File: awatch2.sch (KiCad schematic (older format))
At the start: 0 parts

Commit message: add sensors
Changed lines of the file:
@@
 F35 "NRF_CHICKEN3" B L 3500 4400 50
 F36 "PMIC_INTn" I L 3500 3800 50
+F37 "SENS_IMU_INT" I R 5000 4100 50
 $EndSheet
 $Sheet
@@
 	5300 2300 5000 2300
 $Sheet
-S 5250 3800 750  600
+S 5250 3800 700  400
 U 5C3CD34E
 F0 "Sensors" 50
 F1 "awatch-sensors.sch" 50
+F2 "SENS_SCL" I L 5250 3900 50
+F3 "SENS_SDA" B L 5250 4000 50
+F4 "SENS_IMU_INT" O L 5250 4100 50
 $EndSheet
+Wire Wire Line
+	5250 3900 5000 3900
+Wire Wire Line
+	5250 4000 5000 4000
+Wire Wire Line
+	5250 4100 5000 4100
 $EndSCHEMATC

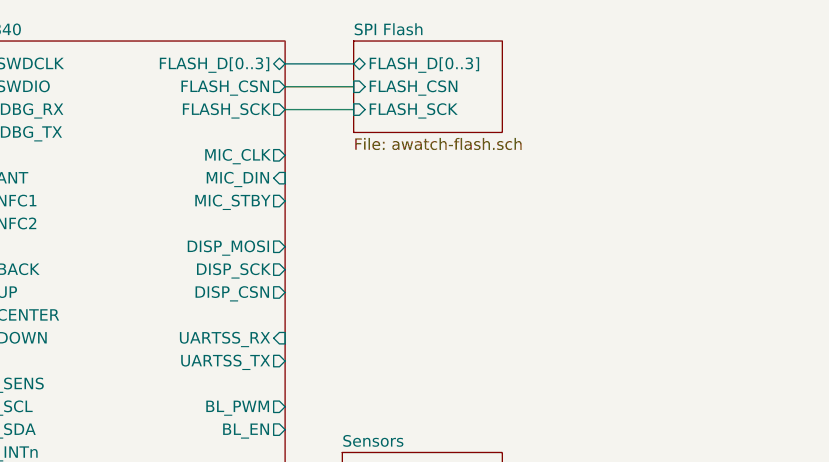
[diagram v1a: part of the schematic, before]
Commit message: add mic
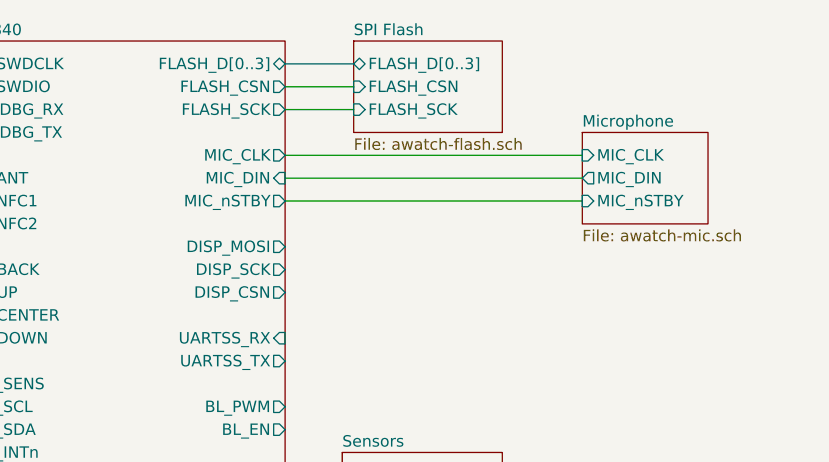
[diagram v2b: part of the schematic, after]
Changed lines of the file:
@@
 $Descr A4 11693 8268
 encoding utf-8
-Sheet 1 5
+Sheet 1 6
 Title "AWatch2"
 Date ""
@@
 F13 "MIC_CLK" O R 5000 2500 50
 F14 "MIC_DIN" I R 5000 2600 50
-F15 "MIC_STBY" O R 5000 2700 50
+F15 "MIC_nSTBY" O R 5000 2700 50
 F16 "PMIC_SCL" O L 3500 3600 50
 F17 "PMIC_SDA" B L 3500 3700 50
@@
 Wire Wire Line
 	5250 4100 5000 4100
+$Sheet
+S 6300 2400 550  400
+U 5C4541B3
+F0 "Microphone" 50
+F1 "awatch-mic.sch" 50
+F2 "MIC_nSTBY" I L 6300 2700 50
+F3 "MIC_CLK" I L 6300 2500 50
+F4 "MIC_DIN" O L 6300 2600 50
+$EndSheet
+Wire Wire Line
+	6300 2500 5000 2500
+Wire Wire Line
+	5000 2600 6300 2600
+Wire Wire Line
+	6300 2700 5000 2700
 $EndSCHEMATC

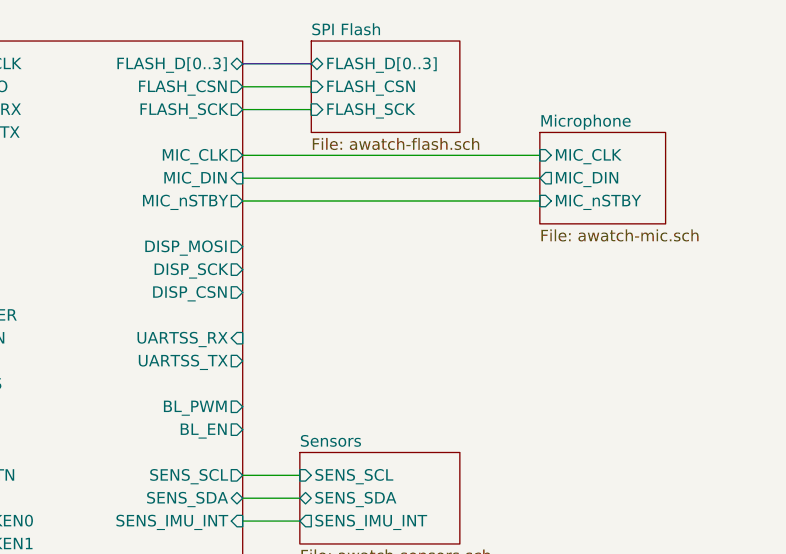
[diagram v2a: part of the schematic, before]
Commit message: Add display.  Add +3.3V LDO for backlight.
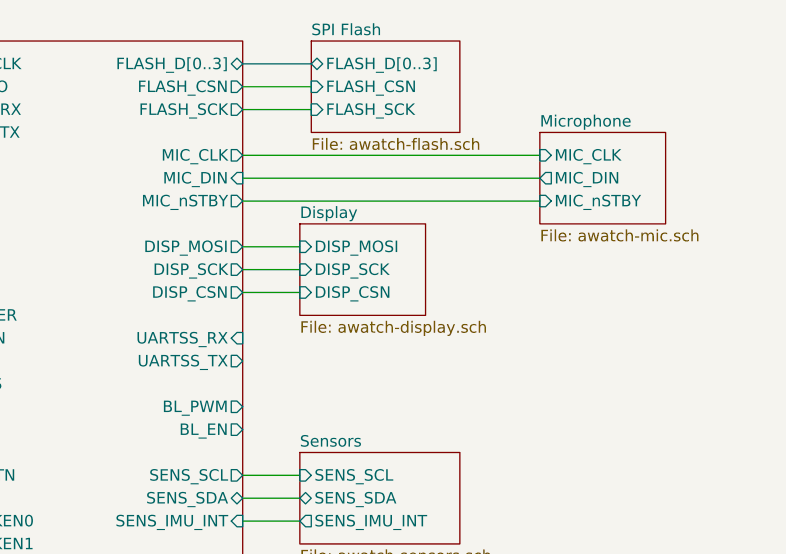
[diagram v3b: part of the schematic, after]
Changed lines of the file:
@@
 $Descr A4 11693 8268
 encoding utf-8
-Sheet 1 6
+Sheet 1 7
 Title "AWatch2"
 Date ""
@@
 Wire Wire Line
 	6300 2700 5000 2700
+$Sheet
+S 5250 2800 550  400
+U 5C4574A7
+F0 "Display" 50
+F1 "awatch-display.sch" 50
+F2 "DISP_MOSI" I L 5250 2900 50
+F3 "DISP_SCK" I L 5250 3000 50
+F4 "DISP_CSN" I L 5250 3100 50
+$EndSheet
+Wire Wire Line
+	5000 2900 5250 2900
+Wire Wire Line
+	5250 3000 5000 3000
+Wire Wire Line
+	5000 3100 5250 3100
 $EndSCHEMATC

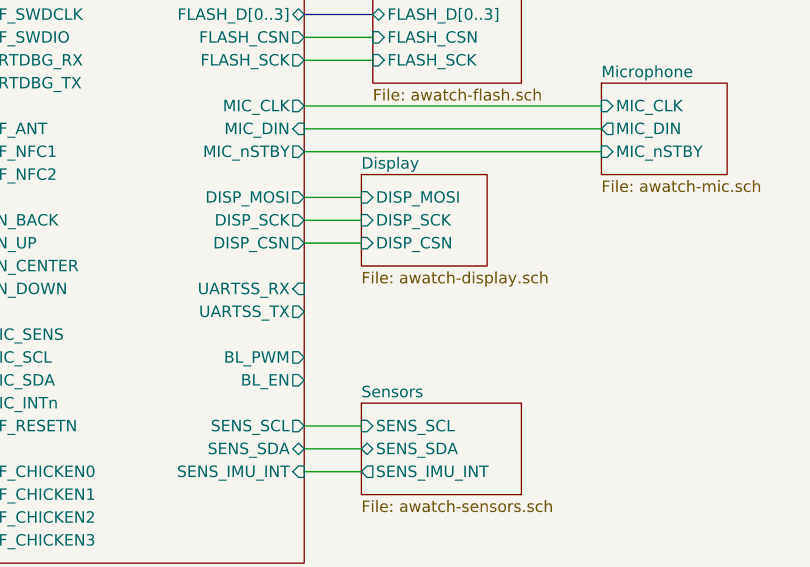
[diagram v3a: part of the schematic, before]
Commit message: backlight PWM through a FET
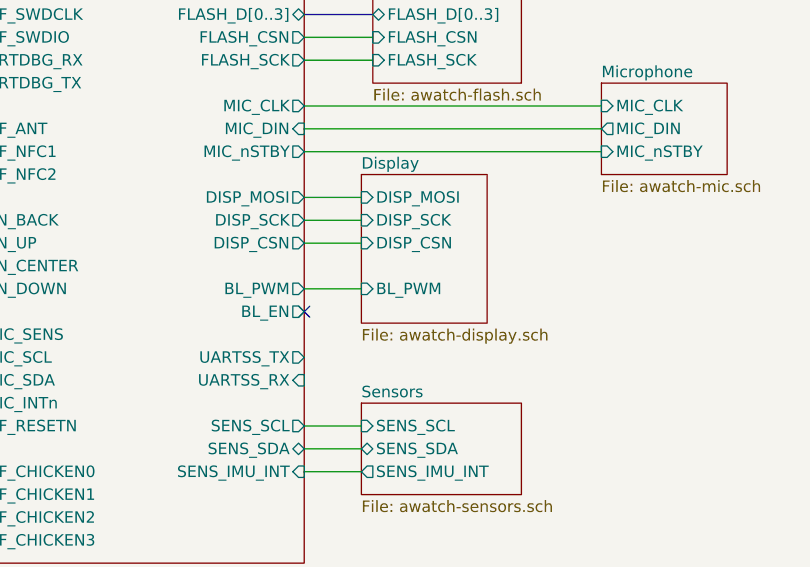
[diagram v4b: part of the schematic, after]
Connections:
- no-connect marks 0 -> 1
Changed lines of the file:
@@
 F19 "DISP_SCK" O R 5000 3000 50
 F20 "DISP_CSN" O R 5000 3100 50
-F21 "UARTSS_RX" I R 5000 3300 50
-F22 "UARTSS_TX" O R 5000 3400 50
+F21 "UARTSS_RX" I R 5000 3700 50
+F22 "UARTSS_TX" O R 5000 3600 50
 F23 "UARTDBG_RX" I L 3500 2300 50
 F24 "UARTDBG_TX" O L 3500 2400 50
-F25 "BL_PWM" O R 5000 3600 50
-F26 "BL_EN" O R 5000 3700 50
+F25 "BL_PWM" O R 5000 3300 50
+F26 "BL_EN" O R 5000 3400 50
 F27 "SENS_SCL" O R 5000 3900 50
 F28 "SENS_SDA" B R 5000 4000 50
@@
 	6300 2700 5000 2700
 $Sheet
-S 5250 2800 550  400
+S 5250 2800 550  650
 U 5C4574A7
 F0 "Display" 50
@@
 F3 "DISP_SCK" I L 5250 3000 50
 F4 "DISP_CSN" I L 5250 3100 50
+F5 "BL_PWM" I L 5250 3300 50
 $EndSheet
 Wire Wire Line
@@
 Wire Wire Line
 	5000 3100 5250 3100
+Wire Wire Line
+	5000 3300 5250 3300
+NoConn ~ 5000 3400
 $EndSCHEMATC

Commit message: add FTDI
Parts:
- added J? (x3): Conn_01x02, symbol Connector_Generic:Conn_01x02
- added SW? (x4): SW_Push, symbol Switch:SW_Push
- added TP? (x7): TestPoint, symbol Connector:TestPoint
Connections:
- net PMIC/BAT+: now also J?.2 (Pin_2)
- net PMIC/BAT-: now also J?.1 (Pin_1), J?.1 (Pin_1)
- net PMIC/BAT_THM: now also J?.2 (Pin_2)
- net PMIC/BTN_BACK: now also SW?.2
- net Sensors/SENS_SCL: now also TP?.1
- net Sensors/SENS_SDA: now also TP?.1
- net nRF52840/BTN_CENTER: now also SW?.2
- net nRF52840/BTN_DOWN: now also SW?.2
- net nRF52840/BTN_UP: now also SW?.2
- net nRF52840/NRF_ANT: now also TP?.1
- net nRF52840/NRF_CHICKEN0: now also TP?.1
- net nRF52840/NRF_CHICKEN1: now also TP?.1
- net nRF52840/NRF_CHICKEN2: now also TP?.1
- net nRF52840/NRF_CHICKEN3: now also TP?.1
- net nRF52840/NRF_NFC1: now also J?.2 (Pin_2)
- net nRF52840/NRF_NFC2: now also J?.1 (Pin_1)
- new net GND: SW?.1, SW?.1, SW?.1, SW?.1
- no-connect marks 1 -> 3

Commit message: add vibrate
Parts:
- added J?: Conn_01x02, symbol Connector_Generic:Conn_01x02
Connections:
- new net Vibrate motor driver/VIBE_OUT+: J?.2 (Pin_2)
- new net Vibrate motor driver/VIBE_OUT-: J?.1 (Pin_1)
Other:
- moved on the sheet: J?, SW?, TP?

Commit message: annotate all
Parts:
- gave numbers to parts that had none: 15
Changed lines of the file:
@@
 	5150 2250 4750 2250
 $Comp
-L Connector:TestPoint TP?
+L Connector:TestPoint TP101
 U 1 1 5C7B2BD0
 P 4950 3950
-F 0 "TP?" V 5145 4024 50  0000 C CNN
+F 0 "TP101" V 5145 4024 50  0000 C CNN
 F 1 "TestPoint" V 5054 4024 50  0000 C CNN
 F 2 "" H 5150 3950 50  0001 C CNN
@@
 	4950 3950 5150 3950
 $Comp
-L Connector:TestPoint TP?
+L Connector:TestPoint TP102
 U 1 1 5C7B30D8
 P 4950 4050
-F 0 "TP?" V 5145 4124 50  0000 C CNN
+F 0 "TP102" V 5145 4124 50  0000 C CNN
 F 1 "TestPoint" V 5054 4124 50  0000 C CNN
 F 2 "" H 5150 4050 50  0001 C CNN
@@
 	4950 4050 5150 4050
 $Comp
-L Connector:TestPoint TP?
+L Connector:TestPoint TP103
 U 1 1 5C7B35EE
 P 4950 4150
-F 0 "TP?" V 5145 4224 50  0000 C CNN
+F 0 "TP103" V 5145 4224 50  0000 C CNN
 F 1 "TestPoint" V 5054 4224 50  0000 C CNN
 F 2 "" H 5150 4150 50  0001 C CNN
@@
 	4950 4150 5150 4150
 $Comp
-L Connector:TestPoint TP?
+L Connector:TestPoint TP104
 U 1 1 5C7B3B74
 P 4950 4250
-F 0 "TP?" V 5145 4324 50  0000 C CNN
+F 0 "TP104" V 5145 4324 50  0000 C CNN
 F 1 "TestPoint" V 5054 4324 50  0000 C CNN
 F 2 "" H 5150 4250 50  0001 C CNN
@@
 	4950 4250 5150 4250
 $Comp
-L Connector:TestPoint TP?
+L Connector:TestPoint TP105
 U 1 1 5C7B41B6
 P 5000 2450
-F 0 "TP?" V 5195 2524 50  0000 C CNN
+F 0 "TP105" V 5195 2524 50  0000 C CNN
 F 1 "TestPoint" V 5104 2524 50  0000 C CNN
 F 2 "" H 5200 2450 50  0001 C CNN
@@
 P 3600 2650
 AR Path="/5C357822/5C7B5026" Ref="J?"  Part="1"
-AR Path="/5C7B5026" Ref="J?"  Part="1"
-F 0 "J?" H 3520 2325 50  0000 C CNN
+AR Path="/5C7B5026" Ref="J104"  Part="1"
+F 0 "J104" H 3520 2325 50  0000 C CNN
 F 1 "Conn_01x02" H 3520 2416 50  0000 C CNN
 F 2 "" H 3600 2650 50  0001 C CNN
@@
 P 2600 2950
 AR Path="/5C357822/5C7B934C" Ref="J?"  Part="1"
-AR Path="/5C7B934C" Ref="J?"  Part="1"
-F 0 "J?" H 2520 2625 50  0000 C CNN
+AR Path="/5C7B934C" Ref="J102"  Part="1"
+F 0 "J102" H 2520 2625 50  0000 C CNN
 F 1 "Conn_01x02" H 2520 2716 50  0000 C CNN
 F 2 "" H 2600 2950 50  0001 C CNN
@@
 P 2600 3400
 AR Path="/5C357822/5C7BAE8F" Ref="J?"  Part="1"
-AR Path="/5C7BAE8F" Ref="J?"  Part="1"
-F 0 "J?" H 2520 3075 50  0000 C CNN
+AR Path="/5C7BAE8F" Ref="J103"  Part="1"
+F 0 "J103" H 2520 3075 50  0000 C CNN
 F 1 "Conn_01x02" H 2520 3166 50  0000 C CNN
 F 2 "" H 2600 3400 50  0001 C CNN
@@
 	4550 5800 4450 5800
 $Comp
-L power:GND #PWR?
+L power:GND #PWR0119
 U 1 1 5C7C612C
 P 4650 5900
-F 0 "#PWR?" H 4650 5650 50  0001 C CNN
+F 0 "#PWR0119" H 4650 5650 50  0001 C CNN
 F 1 "GND" H 4655 5727 50  0000 C CNN
 F 2 "" H 4650 5900 50  0001 C CNN
@@
 Connection ~ 4650 5800
 $Comp
-L Switch:SW_Push SW?
+L Switch:SW_Push SW101
 U 1 1 5C7C7C50
 P 4350 5400
-F 0 "SW?" V 4396 5352 50  0000 R CNN
+F 0 "SW101" V 4396 5352 50  0000 R CNN
 F 1 "SW_Push" V 4305 5352 50  0000 R CNN
 F 2 "" H 4350 5600 50  0001 C CNN
@@
 $EndComp
 $Comp
-L Switch:SW_Push SW?
+L Switch:SW_Push SW102
 U 1 1 5C7CB63F
 P 4450 5400
-F 0 "SW?" V 4496 5352 50  0000 R CNN
+F 0 "SW102" V 4496 5352 50  0000 R CNN
 F 1 "SW_Push" V 4405 5352 50  0000 R CNN
 F 2 "" H 4450 5600 50  0001 C CNN
@@
 $EndComp
 $Comp
-L Switch:SW_Push SW?
+L Switch:SW_Push SW103
 U 1 1 5C7CB661
 P 4550 5400
-F 0 "SW?" V 4596 5352 50  0000 R CNN
+F 0 "SW103" V 4596 5352 50  0000 R CNN
 F 1 "SW_Push" V 4505 5352 50  0000 R CNN
 F 2 "" H 4550 5600 50  0001 C CNN
@@
 $EndComp
 $Comp
-L Switch:SW_Push SW?
+L Switch:SW_Push SW104
 U 1 1 5C7CB685
 P 4650 5400
-F 0 "SW?" V 4696 5352 50  0000 R CNN
+F 0 "SW104" V 4696 5352 50  0000 R CNN
 F 1 "SW_Push" V 4605 5352 50  0000 R CNN
 F 2 "" H 4650 5600 50  0001 C CNN
@@
 	6650 3950 7250 3950
 $Comp
-L Connector:TestPoint TP?
+L Connector:TestPoint TP106
 U 1 1 5C7D0B25
 P 6850 4100
-F 0 "TP?" H 6792 4127 50  0000 R CNN
+F 0 "TP106" H 6792 4127 50  0000 R CNN
 F 1 "TestPoint" H 6792 4218 50  0000 R CNN
 F 2 "" H 7050 4100 50  0001 C CNN
@@
 	6850 3750 7250 3750
 $Comp
-L Connector:TestPoint TP?
+L Connector:TestPoint TP107
 U 1 1 5C7D1D36
 P 6950 4100
-F 0 "TP?" H 6892 4127 50  0000 R CNN
+F 0 "TP107" H 6892 4127 50  0000 R CNN
 F 1 "TestPoint" H 6892 4218 50  0000 R CNN
 F 2 "" H 7150 4100 50  0001 C CNN
@@
 P 2500 4400
 AR Path="/5C357822/5C7D74BF" Ref="J?"  Part="1"
-AR Path="/5C7D74BF" Ref="J?"  Part="1"
-F 0 "J?" H 2420 4075 50  0000 C CNN
+AR Path="/5C7D74BF" Ref="J101"  Part="1"
+F 0 "J101" H 2420 4075 50  0000 C CNN
 F 1 "Conn_01x02" H 2420 4166 50  0000 C CNN
 F 2 "" H 2500 4400 50  0001 C CNN

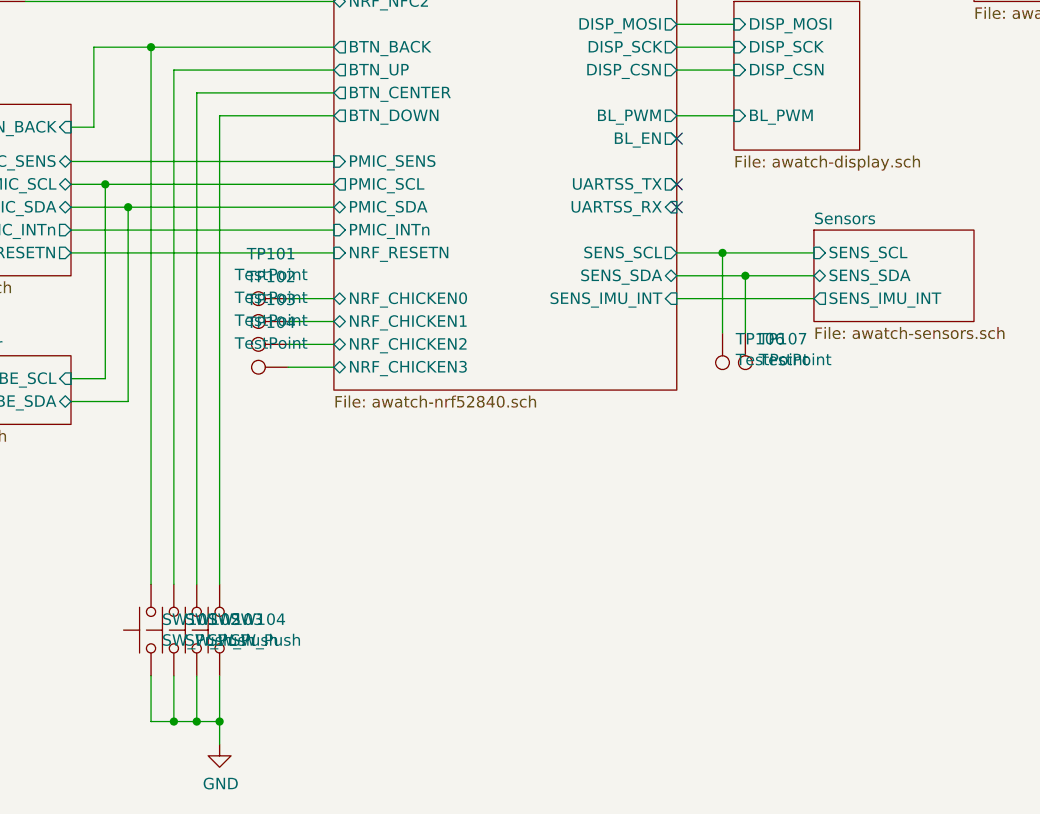
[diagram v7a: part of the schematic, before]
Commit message: Add footprints.
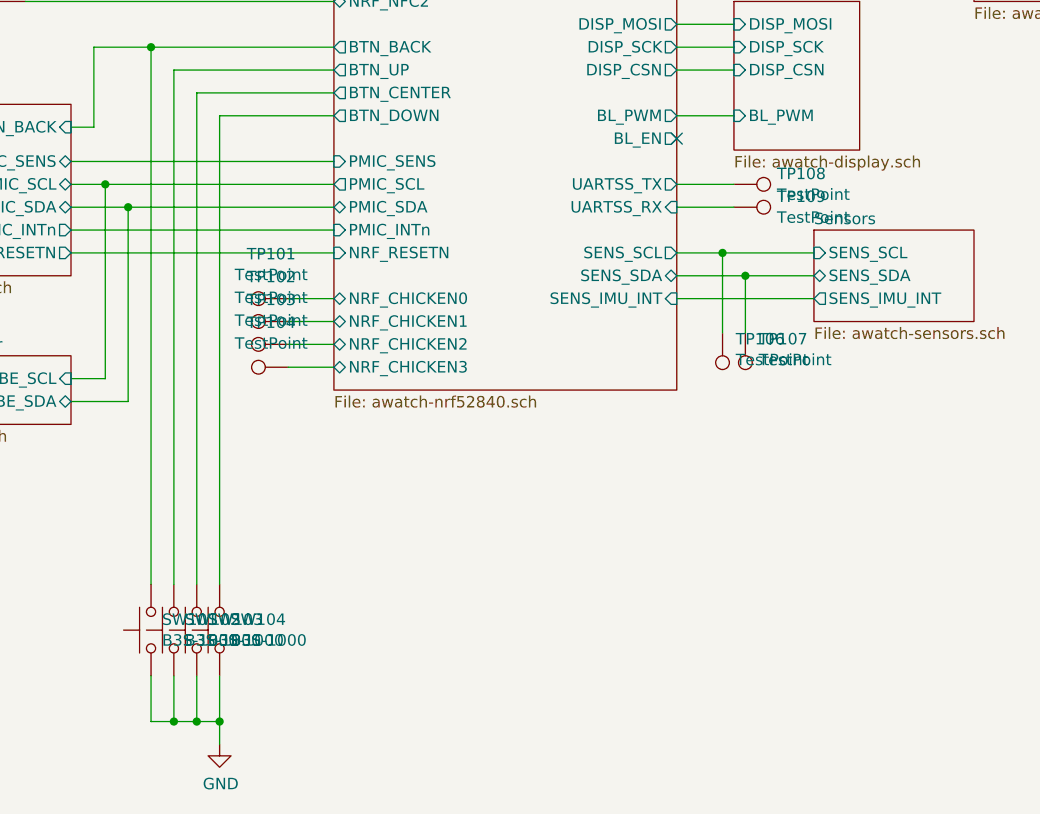
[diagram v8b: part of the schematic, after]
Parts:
- added TP108, TP109: TestPoint, TestPoint:TestPoint_Pad_D1.5mm, symbol Connector:TestPoint
- J101, J102, J103, J104: footprint (none) -> Connector_PinSocket_2.54mm:PinSocket_1x02_P2.54mm_Vertical
- SW101, SW102, SW103, SW104: value SW_Push -> B3S-1000; footprint (none) -> Button_Switch_SMD:SW_SPST_B3S-1000
- TP101, TP102, TP103, TP104, TP105, TP106, TP107: footprint (none) -> TestPoint:TestPoint_Pad_D1.5mm
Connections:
- net nRF52840/UARTSS_RX: now also TP109.1
- net nRF52840/UARTSS_TX: now also TP108.1
- no-connect marks 3 -> 1
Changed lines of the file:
@@
 EESchema Schematic File Version 4
+LIBS:awatch2-cache
 EELAYER 26 0
 EELAYER END
@@
 	6650 3150 6900 3150
 NoConn ~ 6650 3250
-NoConn ~ 6650 3450
-NoConn ~ 6650 3550
 $Sheet
 S 4050 1850 700  500
@@
 F 0 "TP101" V 5145 4024 50  0000 C CNN
 F 1 "TestPoint" V 5054 4024 50  0000 C CNN
-F 2 "" H 5150 3950 50  0001 C CNN
+F 2 "TestPoint:TestPoint_Pad_D1.5mm" H 5150 3950 50  0001 C CNN
 F 3 "~" H 5150 3950 50  0001 C CNN
 	1    4950 3950
@@
 F 0 "TP102" V 5145 4124 50  0000 C CNN
 F 1 "TestPoint" V 5054 4124 50  0000 C CNN
-F 2 "" H 5150 4050 50  0001 C CNN
+F 2 "TestPoint:TestPoint_Pad_D1.5mm" H 5150 4050 50  0001 C CNN
 F 3 "~" H 5150 4050 50  0001 C CNN
 	1    4950 4050
@@
 F 0 "TP103" V 5145 4224 50  0000 C CNN
 F 1 "TestPoint" V 5054 4224 50  0000 C CNN
-F 2 "" H 5150 4150 50  0001 C CNN
+F 2 "TestPoint:TestPoint_Pad_D1.5mm" H 5150 4150 50  0001 C CNN
 F 3 "~" H 5150 4150 50  0001 C CNN
 	1    4950 4150
@@
 F 0 "TP104" V 5145 4324 50  0000 C CNN
 F 1 "TestPoint" V 5054 4324 50  0000 C CNN
-F 2 "" H 5150 4250 50  0001 C CNN
+F 2 "TestPoint:TestPoint_Pad_D1.5mm" H 5150 4250 50  0001 C CNN
 F 3 "~" H 5150 4250 50  0001 C CNN
 	1    4950 4250
@@
 F 0 "TP105" V 5195 2524 50  0000 C CNN
 F 1 "TestPoint" V 5104 2524 50  0000 C CNN
-F 2 "" H 5200 2450 50  0001 C CNN
+F 2 "TestPoint:TestPoint_Pad_D1.5mm" H 5200 2450 50  0001 C CNN
 F 3 "~" H 5200 2450 50  0001 C CNN
 	1    5000 2450
@@
 F 0 "J104" H 3520 2325 50  0000 C CNN
 F 1 "Conn_01x02" H 3520 2416 50  0000 C CNN
-F 2 "" H 3600 2650 50  0001 C CNN
+F 2 "Connector_PinSocket_2.54mm:PinSocket_1x02_P2.54mm_Vertical" H 3600 2650 50  0001 C CNN
 F 3 "~" H 3600 2650 50  0001 C CNN
 	1    3600 2650
@@
 F 0 "J102" H 2520 2625 50  0000 C CNN
 F 1 "Conn_01x02" H 2520 2716 50  0000 C CNN
-F 2 "" H 2600 2950 50  0001 C CNN
+F 2 "Connector_PinSocket_2.54mm:PinSocket_1x02_P2.54mm_Vertical" H 2600 2950 50  0001 C CNN
 F 3 "~" H 2600 2950 50  0001 C CNN
 	1    2600 2950
@@
 F 0 "J103" H 2520 3075 50  0000 C CNN
 F 1 "Conn_01x02" H 2520 3166 50  0000 C CNN
-F 2 "" H 2600 3400 50  0001 C CNN
+F 2 "Connector_PinSocket_2.54mm:PinSocket_1x02_P2.54mm_Vertical" H 2600 3400 50  0001 C CNN
 F 3 "~" H 2600 3400 50  0001 C CNN
 	1    2600 3400
@@
 P 4350 5400
 F 0 "SW101" V 4396 5352 50  0000 R CNN
-F 1 "SW_Push" V 4305 5352 50  0000 R CNN
-F 2 "" H 4350 5600 50  0001 C CNN
+F 1 "B3S-1000" V 4305 5352 50  0000 R CNN
+F 2 "Button_Switch_SMD:SW_SPST_B3S-1000" H 4350 5600 50  0001 C CNN
 F 3 "" H 4350 5600 50  0001 C CNN
 	1    4350 5400
@@
 P 4450 5400
 F 0 "SW102" V 4496 5352 50  0000 R CNN
-F 1 "SW_Push" V 4405 5352 50  0000 R CNN
-F 2 "" H 4450 5600 50  0001 C CNN
+F 1 "B3S-1000" V 4405 5352 50  0000 R CNN
+F 2 "Button_Switch_SMD:SW_SPST_B3S-1000" H 4450 5600 50  0001 C CNN
 F 3 "" H 4450 5600 50  0001 C CNN
 	1    4450 5400
@@
 P 4550 5400
 F 0 "SW103" V 4596 5352 50  0000 R CNN
-F 1 "SW_Push" V 4505 5352 50  0000 R CNN
-F 2 "" H 4550 5600 50  0001 C CNN
+F 1 "B3S-1000" V 4505 5352 50  0000 R CNN
+F 2 "Button_Switch_SMD:SW_SPST_B3S-1000" H 4550 5600 50  0001 C CNN
 F 3 "" H 4550 5600 50  0001 C CNN
 	1    4550 5400
@@
 P 4650 5400
 F 0 "SW104" V 4696 5352 50  0000 R CNN
-F 1 "SW_Push" V 4605 5352 50  0000 R CNN
-F 2 "" H 4650 5600 50  0001 C CNN
+F 1 "B3S-1000" V 4605 5352 50  0000 R CNN
+F 2 "Button_Switch_SMD:SW_SPST_B3S-1000" H 4650 5600 50  0001 C CNN
 F 3 "" H 4650 5600 50  0001 C CNN
 	1    4650 5400
@@
 F 0 "TP106" H 6792 4127 50  0000 R CNN
 F 1 "TestPoint" H 6792 4218 50  0000 R CNN
-F 2 "" H 7050 4100 50  0001 C CNN
+F 2 "TestPoint:TestPoint_Pad_D1.5mm" H 7050 4100 50  0001 C CNN
 F 3 "~" H 7050 4100 50  0001 C CNN
 	1    6850 4100
@@
 F 0 "TP107" H 6892 4127 50  0000 R CNN
 F 1 "TestPoint" H 6892 4218 50  0000 R CNN
-F 2 "" H 7150 4100 50  0001 C CNN
+F 2 "TestPoint:TestPoint_Pad_D1.5mm" H 7150 4100 50  0001 C CNN
 F 3 "~" H 7150 4100 50  0001 C CNN
 	1    6950 4100
@@
 F 0 "J101" H 2420 4075 50  0000 C CNN
 F 1 "Conn_01x02" H 2420 4166 50  0000 C CNN
-F 2 "" H 2500 4400 50  0001 C CNN
+F 2 "Connector_PinSocket_2.54mm:PinSocket_1x02_P2.54mm_Vertical" H 2500 4400 50  0001 C CNN
 F 3 "~" H 2500 4400 50  0001 C CNN
 	1    2500 4400
@@
 Wire Wire Line
 	4250 3550 5150 3550
+$Comp
+L Connector:TestPoint TP108
+U 1 1 5C872B8C
+P 6900 3450
+F 0 "TP108" V 6854 3638 50  0000 L CNN
+F 1 "TestPoint" V 6945 3638 50  0000 L CNN
+F 2 "TestPoint:TestPoint_Pad_D1.5mm" H 7100 3450 50  0001 C CNN
+F 3 "~" H 7100 3450 50  0001 C CNN
+	1    6900 3450
+	0    1    1    0
+$EndComp
+$Comp
+L Connector:TestPoint TP109
+U 1 1 5C872C02
+P 6900 3550
+F 0 "TP109" V 6854 3738 50  0000 L CNN
+F 1 "TestPoint" V 6945 3738 50  0000 L CNN
+F 2 "TestPoint:TestPoint_Pad_D1.5mm" H 7100 3550 50  0001 C CNN
+F 3 "~" H 7100 3550 50  0001 C CNN
+	1    6900 3550
+	0    1    1    0
+$EndComp
+Wire Wire Line
+	6650 3550 6900 3550
+Wire Wire Line
+	6900 3450 6650 3450
 $EndSCHEMATC
